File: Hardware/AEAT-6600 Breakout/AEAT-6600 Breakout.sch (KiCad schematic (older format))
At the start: 14 parts, among them J1 Conn_01x07, J2 Conn_01x09, U1 AEAT-6600-T16

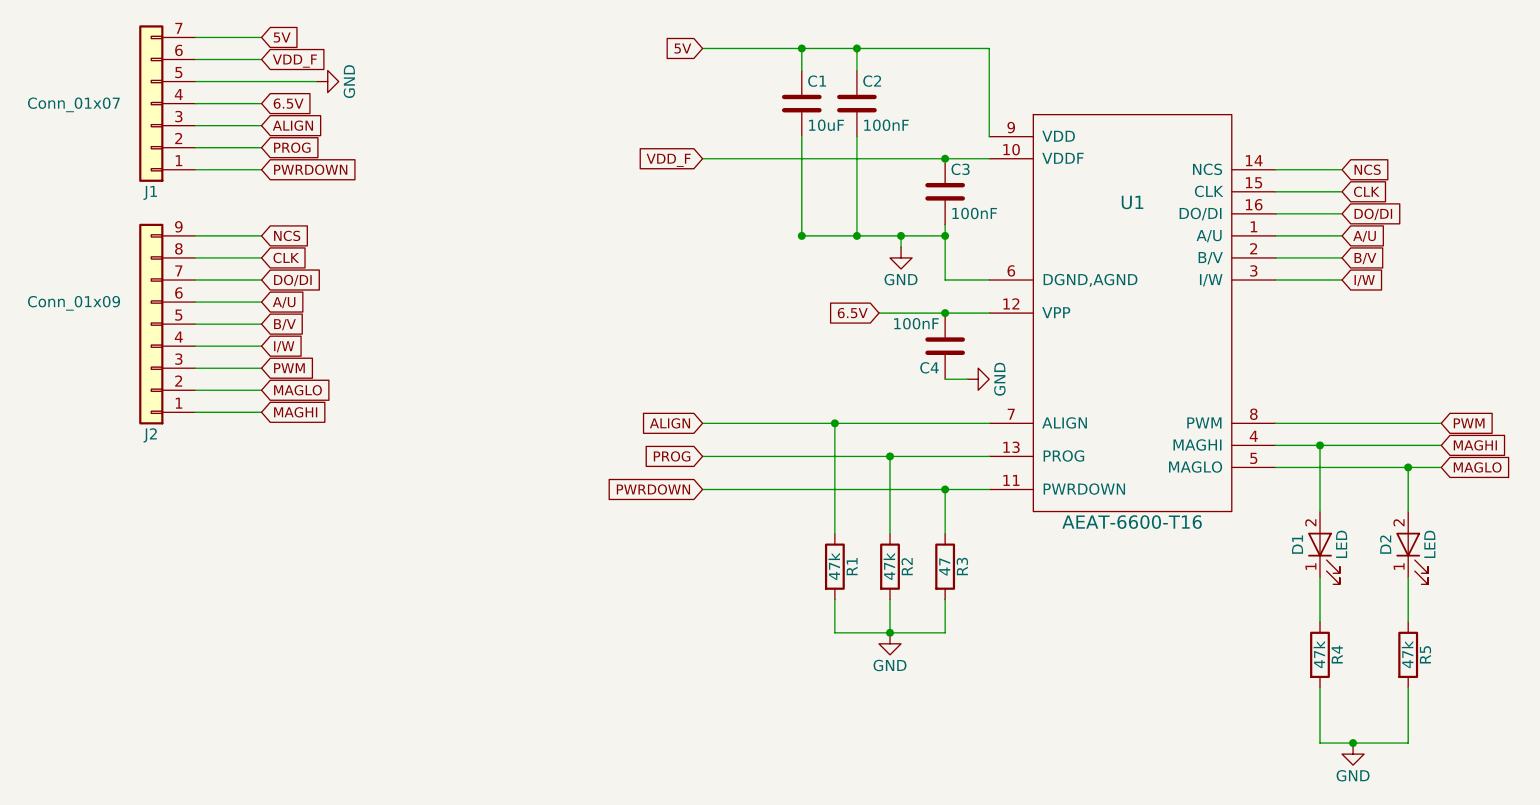
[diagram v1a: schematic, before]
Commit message: Completed breakout boards and BOM
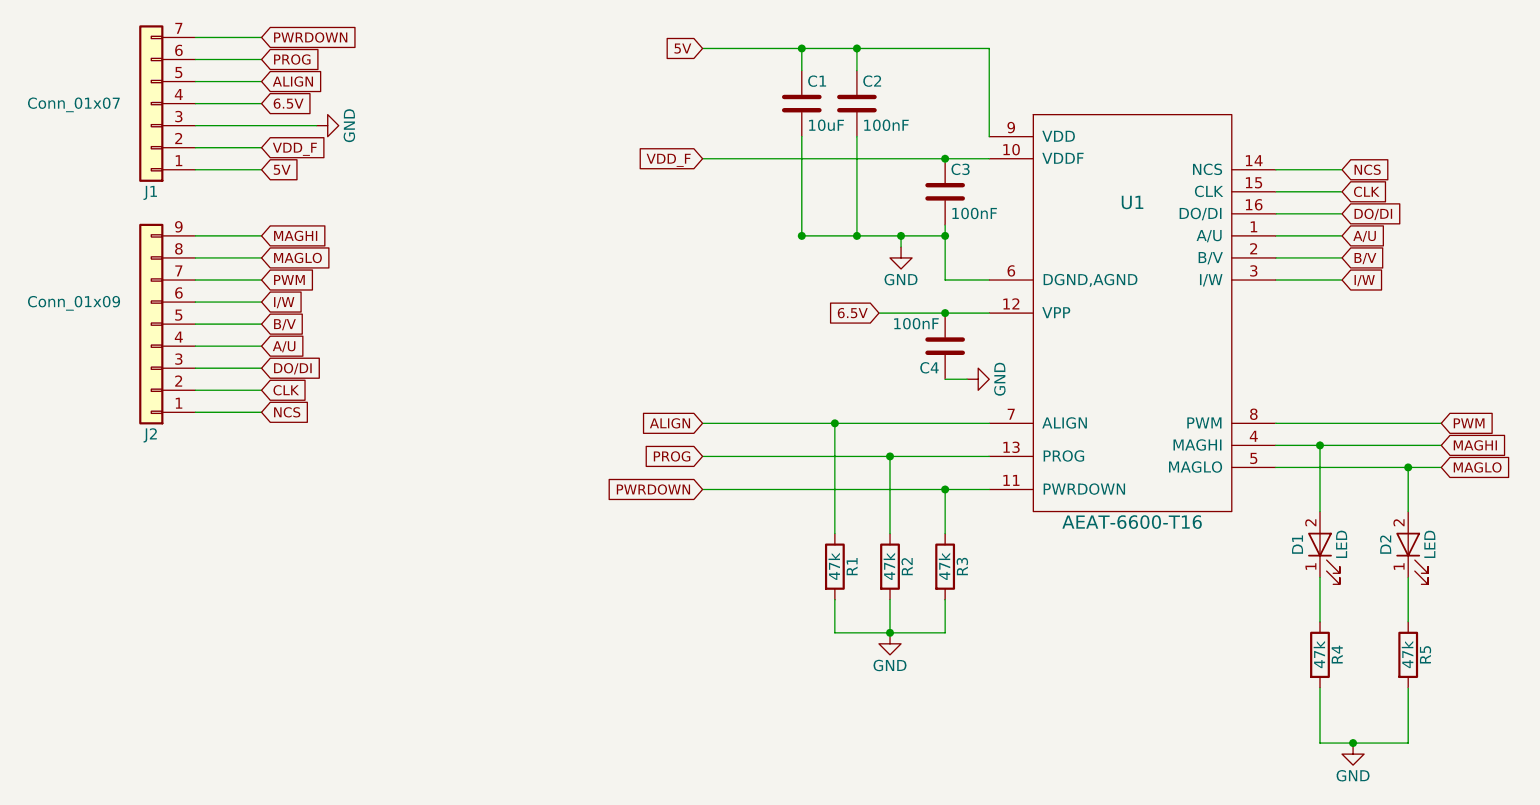
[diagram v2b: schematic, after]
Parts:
- C1: Cost Each (none) -> 0.166; Supplier (none) -> Digikey; Supplier Part Number (none) -> 1276-1096-1-ND
- C2: Cost Each (none) -> 0.064; Supplier RRRR -> Digikey; Supplier Part Number (none) -> 1276-1007-1-ND
- D1: Cost Each (none) -> 0.437; Supplier (none) -> Digikey; Supplier Part Number (none) -> 475-3118-1-ND
- J1, J2: Cost Each (none) -> 1.047; Supplier (none) -> Digikey; Supplier Part Number (none) -> 732-5342-ND
- R3: value 47 -> 47k
- R4: Cost Each (none) -> 0.056; Supplier (none) -> Digikey; Supplier Part Number (none) -> 311-47.0KCRCT-ND
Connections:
- net 5V: now also J1.1 (Pin_1); no longer J1.7 (Pin_7)
- net A/U: now also J2.4 (Pin_4); no longer J2.6 (Pin_6)
- net ALIGN: now also J1.5 (Pin_5); no longer J1.3 (Pin_3)
- net CLK: now also J2.2 (Pin_2); no longer J2.8 (Pin_8)
- net DO/DI: now also J2.3 (Pin_3); no longer J2.7 (Pin_7)
- net GND: now also J1.3 (Pin_3); no longer J1.5 (Pin_5)
- net I/W: now also J2.6 (Pin_6); no longer J2.4 (Pin_4)
- net MAGHI: now also J2.9 (Pin_9); no longer J2.1 (Pin_1)
- net MAGLO: now also J2.8 (Pin_8); no longer J2.2 (Pin_2)
- net NCS: now also J2.1 (Pin_1); no longer J2.9 (Pin_9)
- net PROG: now also J1.6 (Pin_6); no longer J1.2 (Pin_2)
- net PWM: now also J2.7 (Pin_7); no longer J2.3 (Pin_3)
- net PWRDOWN: now also J1.7 (Pin_7); no longer J1.1 (Pin_1)
- net VDD_F: now also J1.2 (Pin_2); no longer J1.6 (Pin_6)
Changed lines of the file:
@@
 F 2 "Capacitors_SMD:C_0805" H 5938 2050 50  0001 C CNN
 F 3 "" H 5900 2200 50  0001 C CNN
-F 4 "RRRR" H 5900 2200 60  0001 C CNN "Supplier"
+F 4 "Digikey" H 5900 2200 60  0001 C CNN "Supplier"
+F 5 "1276-1007-1-ND" H 5900 2200 60  0001 C CNN "Supplier Part Number"
+F 6 "0.064" H 5900 2200 60  0001 C CNN "Cost Each"
 	1    5900 2200
 	1    0    0    -1
@@
 F 2 "Capacitors_SMD:C_0805" H 5688 2050 50  0001 C CNN
 F 3 "" H 5650 2200 50  0001 C CNN
+F 4 "Digikey" H 5650 2200 60  0001 C CNN "Supplier"
+F 5 "1276-1096-1-ND" H 5650 2200 60  0001 C CNN "Supplier Part Number"
+F 6 "0.166" H 5650 2200 60  0001 C CNN "Cost Each"
 	1    5650 2200
 	1    0    0    -1
@@
 P 6300 4300
 F 0 "R3" V 6380 4300 50  0000 C CNN
-F 1 "47" V 6300 4300 50  0000 C CNN
+F 1 "47k" V 6300 4300 50  0000 C CNN
 F 2 "Resistors_SMD:R_0805" V 6230 4300 50  0001 C CNN
 F 3 "" H 6300 4300 50  0001 C CNN
@@
 Text GLabel 8550 3850 2    45   Input ~ 0
 MAGLO
-Text GLabel 3200 1900 2    45   Input ~ 0
+Text GLabel 3200 2500 2    45   Input ~ 0
 5V
-Text GLabel 3200 2000 2    45   Input ~ 0
+Text GLabel 3200 2400 2    45   Input ~ 0
 VDD_F
 Text GLabel 3200 2200 2    45   Input ~ 0
 6.5V
-Text GLabel 3200 2300 2    45   Input ~ 0
+Text GLabel 3200 2100 2    45   Input ~ 0
 ALIGN
-Text GLabel 3200 2400 2    45   Input ~ 0
+Text GLabel 3200 2000 2    45   Input ~ 0
 PROG
-Text GLabel 3200 2500 2    45   Input ~ 0
+Text GLabel 3200 1900 2    45   Input ~ 0
 PWRDOWN
-Text GLabel 3200 2800 2    45   Input ~ 0
+Text GLabel 3200 3600 2    45   Input ~ 0
 NCS
-Text GLabel 3200 2900 2    45   Input ~ 0
+Text GLabel 3200 3500 2    45   Input ~ 0
 CLK
-Text GLabel 3200 3000 2    45   Input ~ 0
+Text GLabel 3200 3400 2    45   Input ~ 0
 DO/DI
-Text GLabel 3200 3100 2    45   Input ~ 0
+Text GLabel 3200 3300 2    45   Input ~ 0
 A/U
 Text GLabel 3200 3200 2    45   Input ~ 0
 B/V
-Text GLabel 3200 3300 2    45   Input ~ 0
+Text GLabel 3200 3100 2    45   Input ~ 0
 I/W
-Text GLabel 3200 3400 2    45   Input ~ 0
+Text GLabel 3200 3000 2    45   Input ~ 0
 PWM
-Text GLabel 3200 3600 2    45   Input ~ 0
+Text GLabel 3200 2800 2    45   Input ~ 0
 MAGHI
-Text GLabel 3200 3500 2    45   Input ~ 0
+Text GLabel 3200 2900 2    45   Input ~ 0
 MAGLO
 $Comp
@@
 F 2 "Pin_Headers:Pin_Header_Angled_1x07_Pitch2.54mm" H 2700 2200 50  0001 C CNN
 F 3 "" H 2700 2200 50  0001 C CNN
+F 4 "Digikey" H 2700 2200 60  0001 C CNN "Supplier"
+F 5 "732-5342-ND" H 2700 2200 60  0001 C CNN "Supplier Part Number"
+F 6 "1.047" H 2700 2200 60  0001 C CNN "Cost Each"
 	1    2700 2200
 	-1   0    0    1
@@
 F 2 "Pin_Headers:Pin_Header_Angled_1x09_Pitch2.54mm" H 2700 3200 50  0001 C CNN
 F 3 "" H 2700 3200 50  0001 C CNN
+F 4 "Digikey" H 2700 3200 60  0001 C CNN "Supplier"
+F 5 "732-5342-ND" H 2700 3200 60  0001 C CNN "Supplier Part Number"
+F 6 "1.047" H 2700 3200 60  0001 C CNN "Cost Each"
 	1    2700 3200
 	-1   0    0    1
@@
 F 2 "Resistors_SMD:R_0805" V 7930 4700 50  0001 C CNN
 F 3 "" H 8000 4700 50  0001 C CNN
+F 4 "Digikey" V 8000 4700 60  0001 C CNN "Supplier"
+F 5 "311-47.0KCRCT-ND" V 8000 4700 60  0001 C CNN "Supplier Part Number"
+F 6 "0.056" V 8000 4700 60  0001 C CNN "Cost Each"
 	1    8000 4700
 	1    0    0    -1
@@
 F 2 "LEDs:LED_0603" H 8000 4200 50  0001 C CNN
 F 3 "" H 8000 4200 50  0001 C CNN
+F 4 "Digikey" H 8000 4200 60  0001 C CNN "Supplier"
+F 5 "475-3118-1-ND" H 8000 4200 60  0001 C CNN "Supplier Part Number"
+F 6 "0.437" H 8000 4200 60  0001 C CNN "Cost Each"
 	1    8000 4200
 	0    -1   -1   0
@@
 	2900 2000 3200 2000
 Wire Wire Line
-	2900 2100 3450 2100
-Wire Wire Line
 	2900 2200 3200 2200
 Wire Wire Line
-	2900 2300 3200 2300
+	2900 2300 3450 2300
 Wire Wire Line
 	3200 2400 2900 2400
@@
 L GND #PWR05
 U 1 1 5B77D87A
-P 3450 2100
-F 0 "#PWR05" H 3450 1850 50  0001 C CNN
-F 1 "GND" H 3450 1950 50  0000 C CNN
-F 2 "" H 3450 2100 50  0001 C CNN
-F 3 "" H 3450 2100 50  0001 C CNN
-	1    3450 2100
+P 3450 2300
+F 0 "#PWR05" H 3450 2050 50  0001 C CNN
+F 1 "GND" H 3450 2150 50  0000 C CNN
+F 2 "" H 3450 2300 50  0001 C CNN
+F 3 "" H 3450 2300 50  0001 C CNN
+	1    3450 2300
 	0    -1   -1   0
 $EndComp
@@
 	6100 2850 6100 2800
 Connection ~ 6100 2800
+Wire Wire Line
+	3200 2100 2900 2100
 $EndSCHEMATC
